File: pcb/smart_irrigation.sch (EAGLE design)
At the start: 31 parts, among them IC1 TMP36, IC2 7805DT, IC3 7833DT, IC4 DS1307, J1 1X2-3.5MM, Q1 IRF730, Q2 32.768, Q3 2N3904, U1 BL600

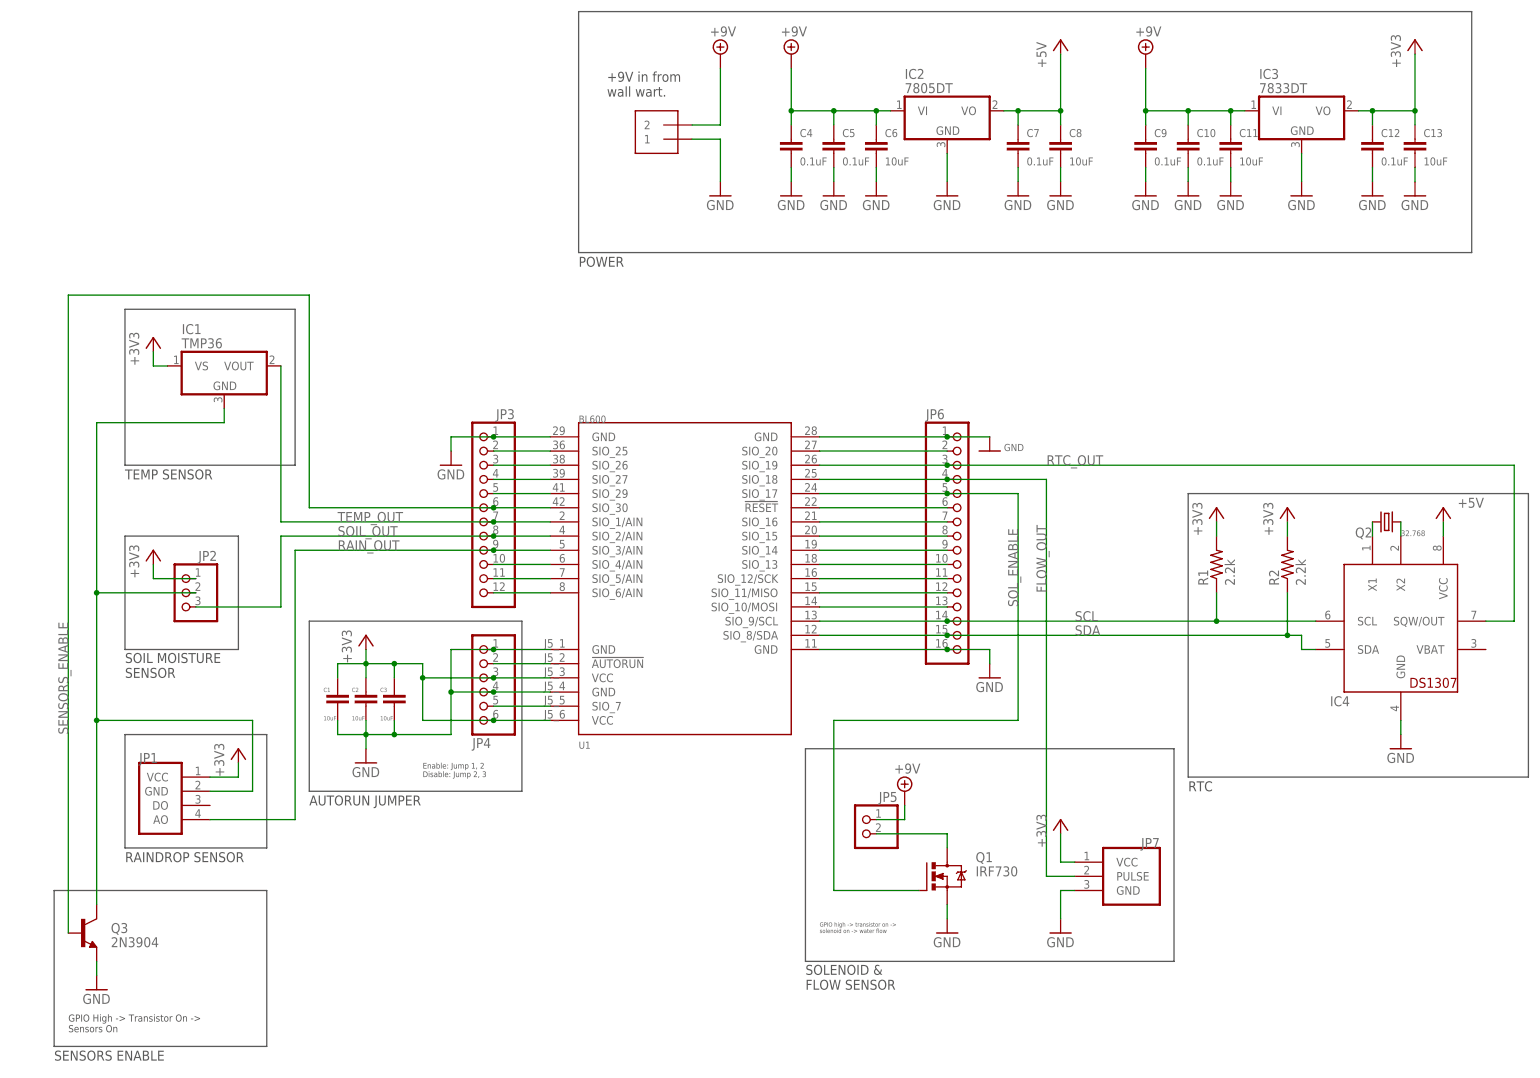
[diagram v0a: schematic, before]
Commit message: PCB: Give names to all signals.
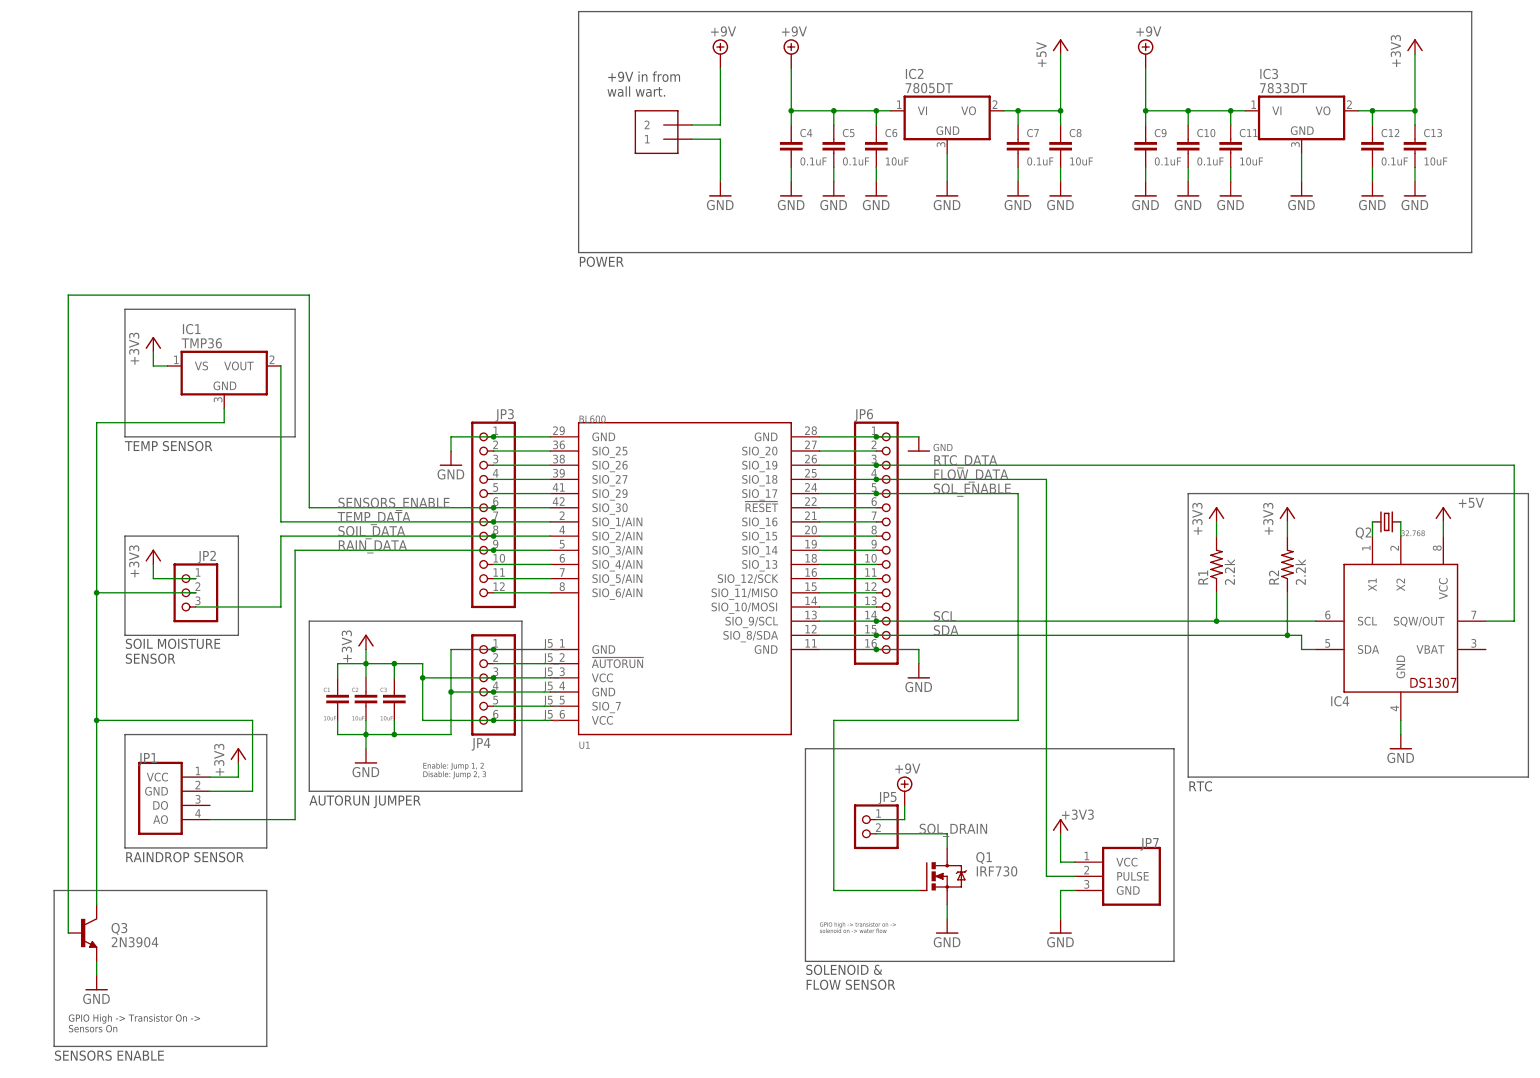
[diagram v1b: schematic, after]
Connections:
- net FLOW_OUT renamed FLOW_DATA
- net N$12 renamed SIO_4
- net N$13 renamed SIO_5
- net N$14 renamed SIO_6
- net N$16 renamed SIO_20
- net N$2 renamed SIO_7
- net N$20 renamed NRESET
- net N$21 renamed SIO_16
- net N$22 renamed SIO_15
- net N$23 renamed SIO_14
- net N$24 renamed SIO_13
- net N$25 renamed SIO_12/SCK
- net N$26 renamed SIO_11/MISO
- net N$27 renamed SIO_10/MOSI
- net N$4 renamed SIO_25
- net N$5 renamed SIO_26
- net N$6 renamed SIO_27
- net N$7 renamed SIO_29
- net RAIN_OUT renamed RAIN_DATA
- net RTC_OUT renamed RTC_DATA
- net SOIL_OUT renamed SOIL_DATA
- net TEMP_OUT renamed TEMP_DATA
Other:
- moved on the sheet: JP6

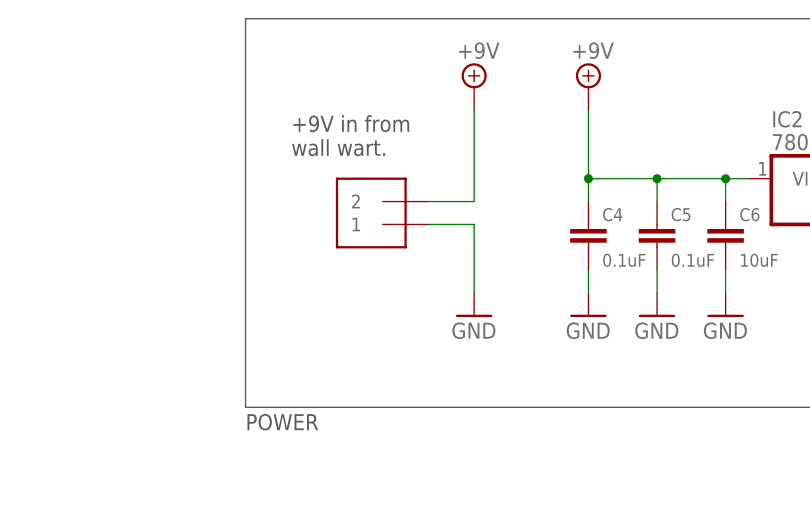
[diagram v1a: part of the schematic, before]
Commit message: PCB: Fix spacing between headers on BL600 package
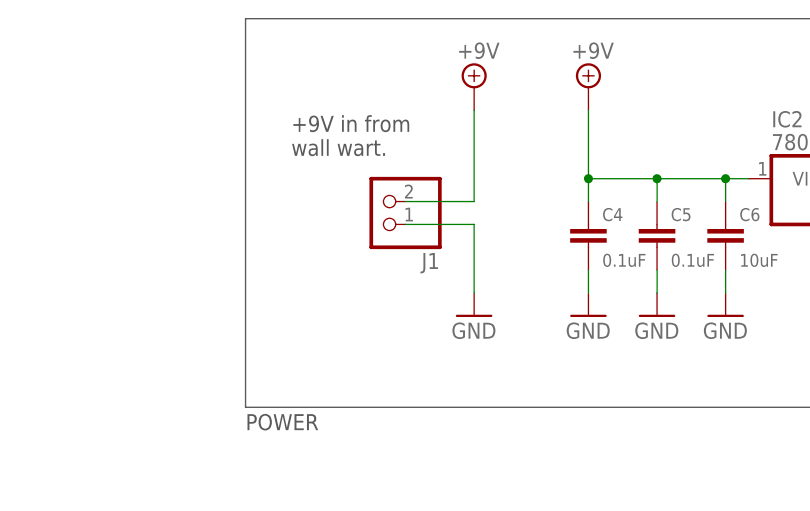
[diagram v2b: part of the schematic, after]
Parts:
- J1: value 1X2-3.5MM -> (none); device adafruit:1X2-3.5MM -> pinhead:PINHD-1X2
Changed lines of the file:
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@@
 <setting verticaltext="up"/>
 </settings>
-<grid distance="0.1" unitdist="inch" unit="inch" style="lines" multiple="1" display="yes" altdistance="0.01" altunitdist="inch" altunit="inch"/>
+<grid distance="0.1" unitdist="inch" unit="inch" style="lines" multiple="1" display="no" altdistance="0.01" altunitdist="inch" altunit="inch"/>
 <layers>
 <layer number="1" name="Top" color="4" fill="1" visible="no" active="no"/>
@@
 <part name="GND8" library="supply1" deviceset="GND" device=""/>
 <part name="GND13" library="supply1" deviceset="GND" device=""/>
-<part name="J1" library="adafruit" deviceset="1X2" device="-3.5MM"/>
+<part name="J1" library="pinhead" deviceset="PINHD-1X2" device=""/>
 <part name="GND4" library="supply1" deviceset="GND" device=""/>
 <part name="C8" library="rcl" deviceset="C-EU" device="C0805" value="10uF"/>
@@
 <pinref part="J1" gate="G$1" pin="1"/>
 <pinref part="GND4" gate="1" pin="GND"/>
-<wire x1="124.46" y1="185.42" x2="129.54" y2="185.42" width="0.1524" layer="91"/>
+<wire x1="121.92" y1="185.42" x2="129.54" y2="185.42" width="0.1524" layer="91"/>
 <wire x1="129.54" y1="185.42" x2="129.54" y2="177.8" width="0.1524" layer="91"/>
 </segment>
@@
 <segment>
 <pinref part="J1" gate="G$1" pin="2"/>
-<wire x1="124.46" y1="187.96" x2="129.54" y2="187.96" width="0.1524" layer="91"/>
+<wire x1="121.92" y1="187.96" x2="129.54" y2="187.96" width="0.1524" layer="91"/>
 <wire x1="129.54" y1="187.96" x2="129.54" y2="198.12" width="0.1524" layer="91"/>
 <pinref part="SUPPLY1" gate="G$1" pin="+9V"/>
